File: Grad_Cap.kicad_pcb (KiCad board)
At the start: 2 copper layers, 2 parts, among them U1 Itsy_NRF

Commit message: Cleaning files
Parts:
- moved U1 214.5 mm to (233.4, 216.5)
- moved D1 22.8 mm to (92.5, 45.5)
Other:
- board outline added: 240 x 240 mm
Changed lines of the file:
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@@
     (thickness 1.6)
   )
-  (paper "A4")
+  (paper "A3")
   (layers
     (0 "F.Cu" signal)
@@
   (net 31 "VBUS")
   (footprint "LED_SMD:LED_Inolux_IN-PI554FCH_PLCC4_5.0x5.0mm_P3.2mm" (layer "F.Cu")
-    (at 103.5 65.5)
+    (at 92.5 45.5)
     (descr "http://www.inolux-corp.com/datasheet/SMDLED/Addressable%20LED/IN-PI554FCH.pdf")
     (tags "RGB LED NeoPixel addressable")
@@
   )
   (footprint "Package_DIP:DIP-28_W15.24mm_LongPads" (layer "F.Cu")
-    (at 82.3 64.3)
+    (at 233.4 216.5)
     (descr "28-lead though-hole mounted DIP package, row spacing 15.24 mm (600 mils), LongPads")
     (tags "THT DIP DIL PDIP 2.54mm 15.24mm 600mil LongPads")
@@
     )
   )
+  (gr_circle (center 140 140) (end 160 140) (layer "Edge.Cuts") (width 0.1) (fill none))
+  (gr_rect (start 20 20) (end 260 260) (layer "Edge.Cuts") (width 0.1) (fill none))
 )

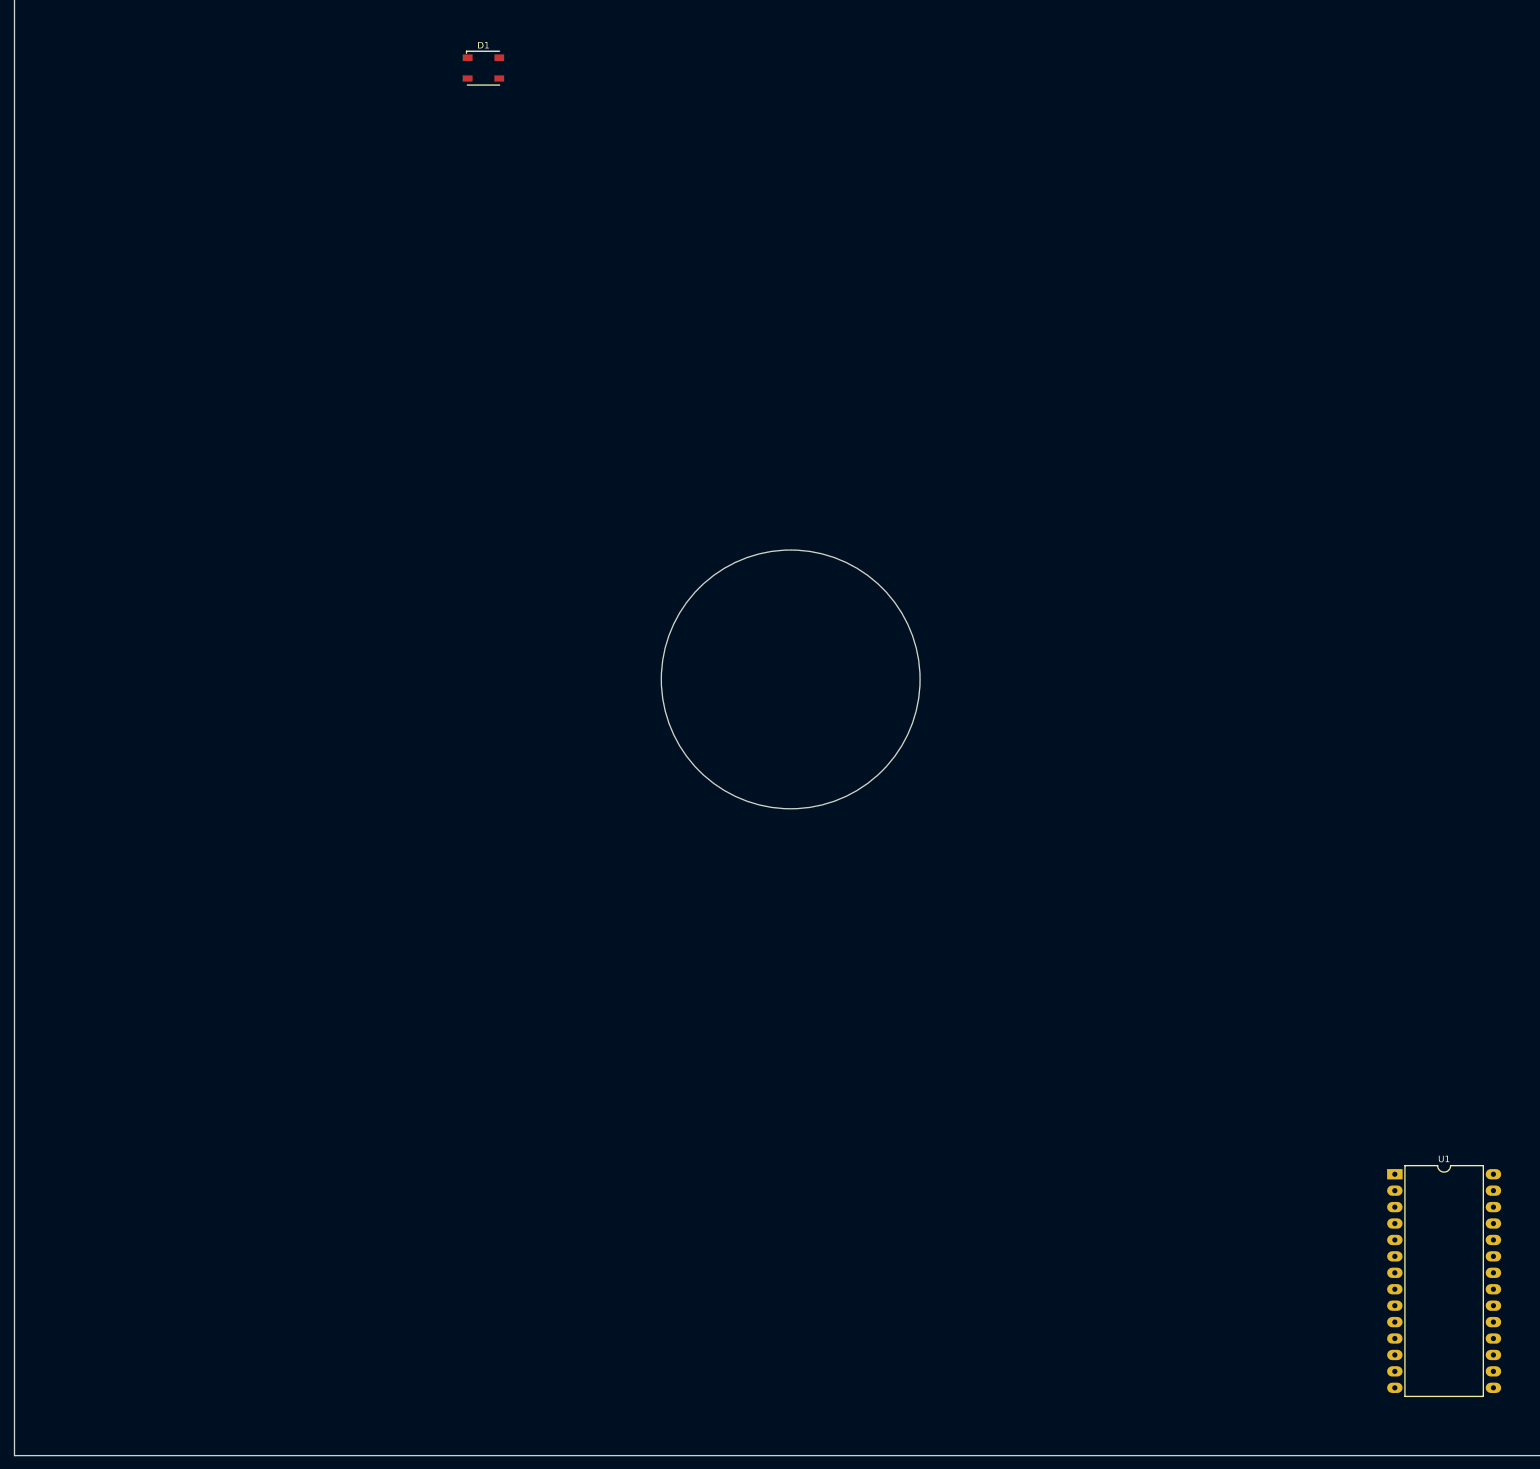
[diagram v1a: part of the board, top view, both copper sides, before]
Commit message: Added neopixels
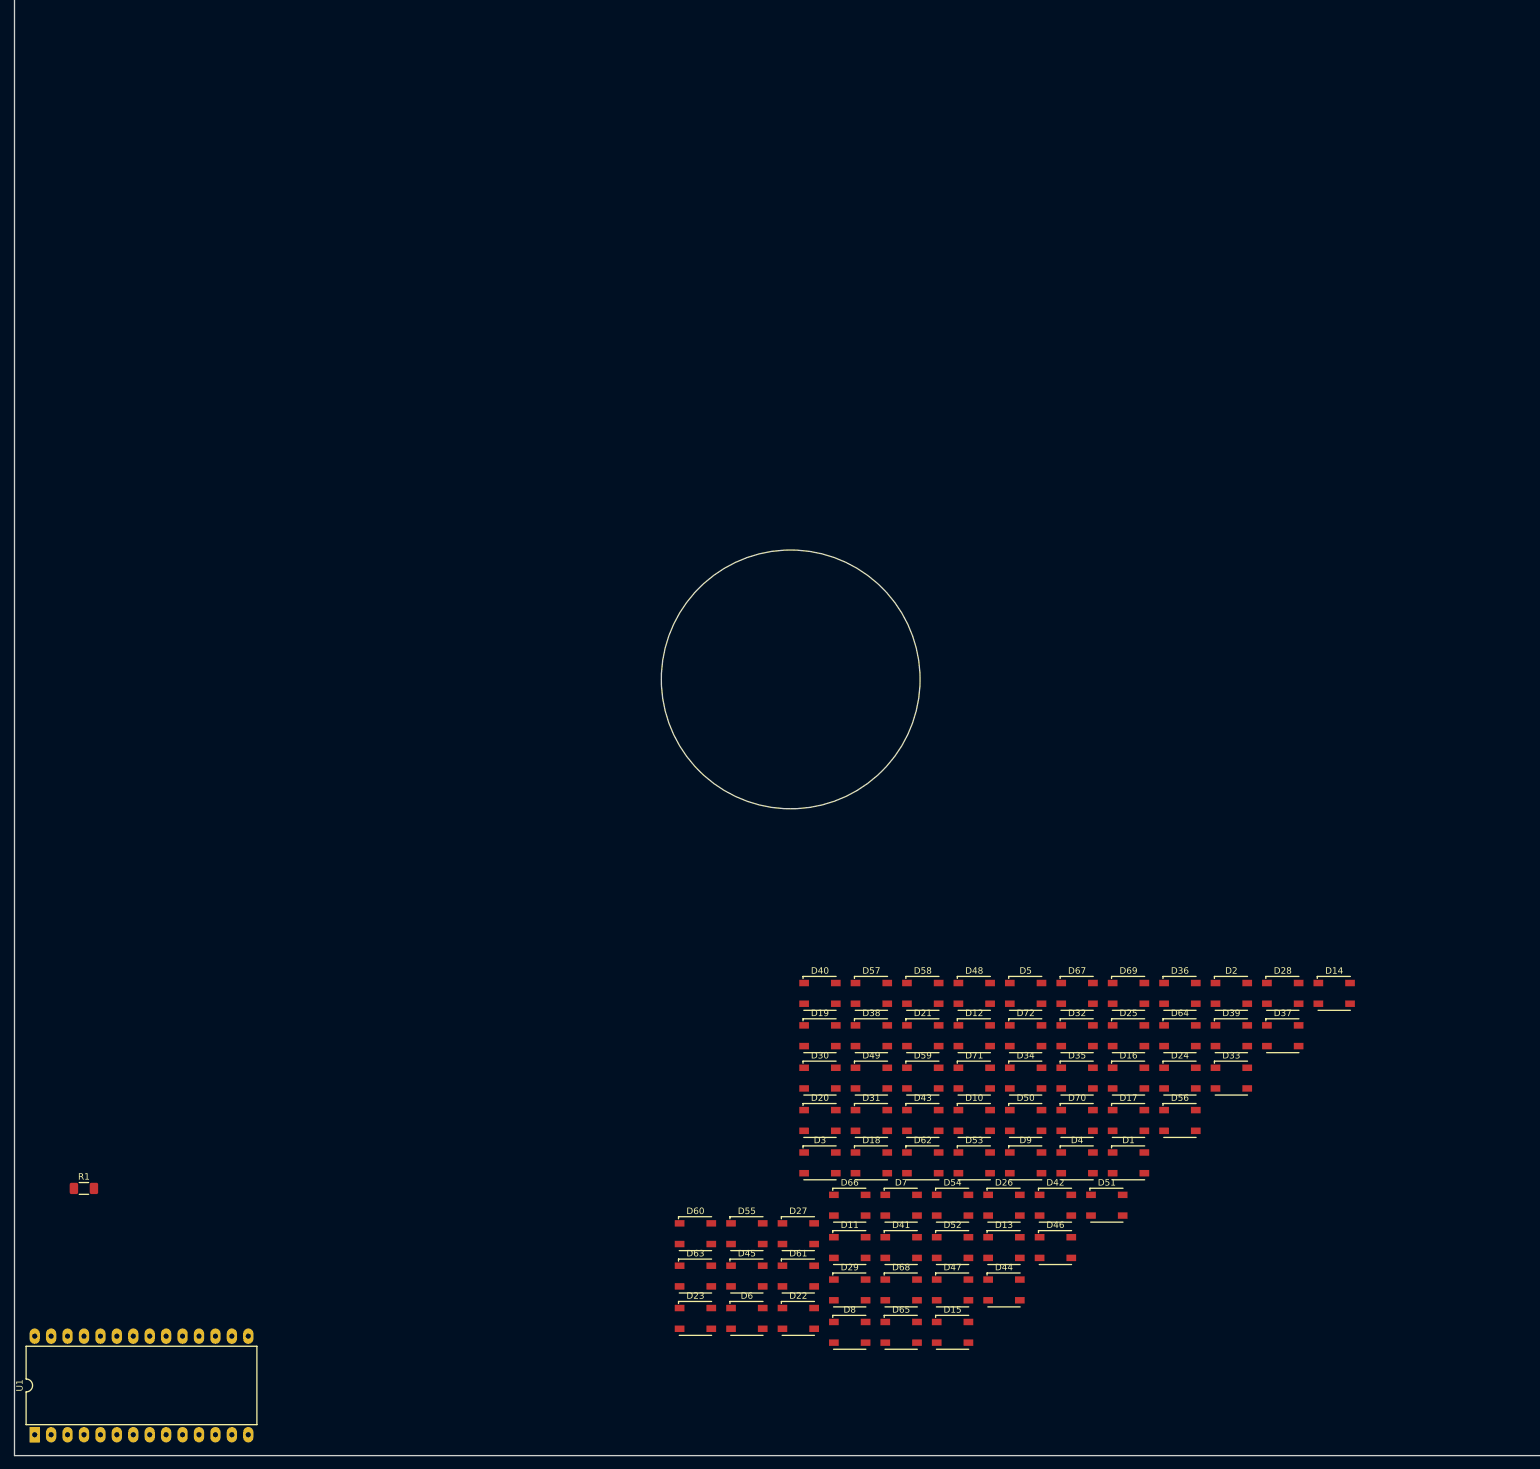
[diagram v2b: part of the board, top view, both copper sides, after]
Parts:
- added D10: Neopixel 5050, LED_SMD:LED_Inolux_IN-PI554FCH_PLCC4_5.0x5.0mm_P3.2mm, F.Cu at (168.4, 208.2)
- added D11: Neopixel 5050, LED_SMD:LED_Inolux_IN-PI554FCH_PLCC4_5.0x5.0mm_P3.2mm, F.Cu at (149.1, 227.8)
- added D12: Neopixel 5050, LED_SMD:LED_Inolux_IN-PI554FCH_PLCC4_5.0x5.0mm_P3.2mm, F.Cu at (168.4, 195.1)
- added D13: Neopixel 5050, LED_SMD:LED_Inolux_IN-PI554FCH_PLCC4_5.0x5.0mm_P3.2mm, F.Cu at (173.0, 227.8)
- added D14: Neopixel 5050, LED_SMD:LED_Inolux_IN-PI554FCH_PLCC4_5.0x5.0mm_P3.2mm, F.Cu at (224.0, 188.5)
- added D15: Neopixel 5050, LED_SMD:LED_Inolux_IN-PI554FCH_PLCC4_5.0x5.0mm_P3.2mm, F.Cu at (165.0, 240.9)
- added D16: Neopixel 5050, LED_SMD:LED_Inolux_IN-PI554FCH_PLCC4_5.0x5.0mm_P3.2mm, F.Cu at (192.2, 201.6)
- added D17: Neopixel 5050, LED_SMD:LED_Inolux_IN-PI554FCH_PLCC4_5.0x5.0mm_P3.2mm, F.Cu at (192.2, 208.2)
- added D18: Neopixel 5050, LED_SMD:LED_Inolux_IN-PI554FCH_PLCC4_5.0x5.0mm_P3.2mm, F.Cu at (152.5, 214.7)
- added D19: Neopixel 5050, LED_SMD:LED_Inolux_IN-PI554FCH_PLCC4_5.0x5.0mm_P3.2mm, F.Cu at (144.5, 195.1)
- added D2: Neopixel 5050, LED_SMD:LED_Inolux_IN-PI554FCH_PLCC4_5.0x5.0mm_P3.2mm, F.Cu at (208.1, 188.5)
- added D20: Neopixel 5050, LED_SMD:LED_Inolux_IN-PI554FCH_PLCC4_5.0x5.0mm_P3.2mm, F.Cu at (144.5, 208.2)
- added D21: Neopixel 5050, LED_SMD:LED_Inolux_IN-PI554FCH_PLCC4_5.0x5.0mm_P3.2mm, F.Cu at (160.4, 195.1)
- added D22: Neopixel 5050, LED_SMD:LED_Inolux_IN-PI554FCH_PLCC4_5.0x5.0mm_P3.2mm, F.Cu at (141.2, 238.8)
- added D23: Neopixel 5050, LED_SMD:LED_Inolux_IN-PI554FCH_PLCC4_5.0x5.0mm_P3.2mm, F.Cu at (125.3, 238.8)
- added D24: Neopixel 5050, LED_SMD:LED_Inolux_IN-PI554FCH_PLCC4_5.0x5.0mm_P3.2mm, F.Cu at (200.2, 201.6)
- added D25: Neopixel 5050, LED_SMD:LED_Inolux_IN-PI554FCH_PLCC4_5.0x5.0mm_P3.2mm, F.Cu at (192.2, 195.1)
- added D26: Neopixel 5050, LED_SMD:LED_Inolux_IN-PI554FCH_PLCC4_5.0x5.0mm_P3.2mm, F.Cu at (173.0, 221.3)
- added D27: Neopixel 5050, LED_SMD:LED_Inolux_IN-PI554FCH_PLCC4_5.0x5.0mm_P3.2mm, F.Cu at (141.2, 225.7)
- added D28: Neopixel 5050, LED_SMD:LED_Inolux_IN-PI554FCH_PLCC4_5.0x5.0mm_P3.2mm, F.Cu at (216.1, 188.5)
- added D29: Neopixel 5050, LED_SMD:LED_Inolux_IN-PI554FCH_PLCC4_5.0x5.0mm_P3.2mm, F.Cu at (149.1, 234.4)
- added D3: Neopixel 5050, LED_SMD:LED_Inolux_IN-PI554FCH_PLCC4_5.0x5.0mm_P3.2mm, F.Cu at (144.5, 214.7)
- added D30: Neopixel 5050, LED_SMD:LED_Inolux_IN-PI554FCH_PLCC4_5.0x5.0mm_P3.2mm, F.Cu at (144.5, 201.6)
- added D31: Neopixel 5050, LED_SMD:LED_Inolux_IN-PI554FCH_PLCC4_5.0x5.0mm_P3.2mm, F.Cu at (152.5, 208.2)
- added D32: Neopixel 5050, LED_SMD:LED_Inolux_IN-PI554FCH_PLCC4_5.0x5.0mm_P3.2mm, F.Cu at (184.3, 195.1)
- added D33: Neopixel 5050, LED_SMD:LED_Inolux_IN-PI554FCH_PLCC4_5.0x5.0mm_P3.2mm, F.Cu at (208.1, 201.6)
- added D34: Neopixel 5050, LED_SMD:LED_Inolux_IN-PI554FCH_PLCC4_5.0x5.0mm_P3.2mm, F.Cu at (176.3, 201.6)
- added D35: Neopixel 5050, LED_SMD:LED_Inolux_IN-PI554FCH_PLCC4_5.0x5.0mm_P3.2mm, F.Cu at (184.3, 201.6)
- added D36: Neopixel 5050, LED_SMD:LED_Inolux_IN-PI554FCH_PLCC4_5.0x5.0mm_P3.2mm, F.Cu at (200.2, 188.5)
- added D37: Neopixel 5050, LED_SMD:LED_Inolux_IN-PI554FCH_PLCC4_5.0x5.0mm_P3.2mm, F.Cu at (216.1, 195.1)
- added D38: Neopixel 5050, LED_SMD:LED_Inolux_IN-PI554FCH_PLCC4_5.0x5.0mm_P3.2mm, F.Cu at (152.5, 195.1)
- added D39: Neopixel 5050, LED_SMD:LED_Inolux_IN-PI554FCH_PLCC4_5.0x5.0mm_P3.2mm, F.Cu at (208.1, 195.1)
- added D4: Neopixel 5050, LED_SMD:LED_Inolux_IN-PI554FCH_PLCC4_5.0x5.0mm_P3.2mm, F.Cu at (184.3, 214.7)
- added D40: Neopixel 5050, LED_SMD:LED_Inolux_IN-PI554FCH_PLCC4_5.0x5.0mm_P3.2mm, F.Cu at (144.5, 188.5)
- added D41: Neopixel 5050, LED_SMD:LED_Inolux_IN-PI554FCH_PLCC4_5.0x5.0mm_P3.2mm, F.Cu at (157.1, 227.8)
- added D42: Neopixel 5050, LED_SMD:LED_Inolux_IN-PI554FCH_PLCC4_5.0x5.0mm_P3.2mm, F.Cu at (180.9, 221.3)
- added D43: Neopixel 5050, LED_SMD:LED_Inolux_IN-PI554FCH_PLCC4_5.0x5.0mm_P3.2mm, F.Cu at (160.4, 208.2)
- added D44: Neopixel 5050, LED_SMD:LED_Inolux_IN-PI554FCH_PLCC4_5.0x5.0mm_P3.2mm, F.Cu at (173.0, 234.4)
- added D45: Neopixel 5050, LED_SMD:LED_Inolux_IN-PI554FCH_PLCC4_5.0x5.0mm_P3.2mm, F.Cu at (133.2, 232.2)
- added D46: Neopixel 5050, LED_SMD:LED_Inolux_IN-PI554FCH_PLCC4_5.0x5.0mm_P3.2mm, F.Cu at (180.9, 227.8)
- added D47: Neopixel 5050, LED_SMD:LED_Inolux_IN-PI554FCH_PLCC4_5.0x5.0mm_P3.2mm, F.Cu at (165.0, 234.4)
- added D48: Neopixel 5050, LED_SMD:LED_Inolux_IN-PI554FCH_PLCC4_5.0x5.0mm_P3.2mm, F.Cu at (168.4, 188.5)
- added D49: Neopixel 5050, LED_SMD:LED_Inolux_IN-PI554FCH_PLCC4_5.0x5.0mm_P3.2mm, F.Cu at (152.5, 201.6)
- added D5: Neopixel 5050, LED_SMD:LED_Inolux_IN-PI554FCH_PLCC4_5.0x5.0mm_P3.2mm, F.Cu at (176.3, 188.5)
- added D50: Neopixel 5050, LED_SMD:LED_Inolux_IN-PI554FCH_PLCC4_5.0x5.0mm_P3.2mm, F.Cu at (176.3, 208.2)
- added D51: Neopixel 5050, LED_SMD:LED_Inolux_IN-PI554FCH_PLCC4_5.0x5.0mm_P3.2mm, F.Cu at (188.9, 221.3)
- added D52: Neopixel 5050, LED_SMD:LED_Inolux_IN-PI554FCH_PLCC4_5.0x5.0mm_P3.2mm, F.Cu at (165.0, 227.8)
- added D53: Neopixel 5050, LED_SMD:LED_Inolux_IN-PI554FCH_PLCC4_5.0x5.0mm_P3.2mm, F.Cu at (168.4, 214.7)
- added D54: Neopixel 5050, LED_SMD:LED_Inolux_IN-PI554FCH_PLCC4_5.0x5.0mm_P3.2mm, F.Cu at (165.0, 221.3)
- added D55: Neopixel 5050, LED_SMD:LED_Inolux_IN-PI554FCH_PLCC4_5.0x5.0mm_P3.2mm, F.Cu at (133.2, 225.7)
- added D56: Neopixel 5050, LED_SMD:LED_Inolux_IN-PI554FCH_PLCC4_5.0x5.0mm_P3.2mm, F.Cu at (200.2, 208.2)
- added D57: Neopixel 5050, LED_SMD:LED_Inolux_IN-PI554FCH_PLCC4_5.0x5.0mm_P3.2mm, F.Cu at (152.5, 188.5)
- added D58: Neopixel 5050, LED_SMD:LED_Inolux_IN-PI554FCH_PLCC4_5.0x5.0mm_P3.2mm, F.Cu at (160.4, 188.5)
- added D59: Neopixel 5050, LED_SMD:LED_Inolux_IN-PI554FCH_PLCC4_5.0x5.0mm_P3.2mm, F.Cu at (160.4, 201.6)
- added D6: Neopixel 5050, LED_SMD:LED_Inolux_IN-PI554FCH_PLCC4_5.0x5.0mm_P3.2mm, F.Cu at (133.2, 238.8)
- added D60: Neopixel 5050, LED_SMD:LED_Inolux_IN-PI554FCH_PLCC4_5.0x5.0mm_P3.2mm, F.Cu at (125.3, 225.7)
- added D61: Neopixel 5050, LED_SMD:LED_Inolux_IN-PI554FCH_PLCC4_5.0x5.0mm_P3.2mm, F.Cu at (141.2, 232.2)
- added D62: Neopixel 5050, LED_SMD:LED_Inolux_IN-PI554FCH_PLCC4_5.0x5.0mm_P3.2mm, F.Cu at (160.4, 214.7)
- added D63: Neopixel 5050, LED_SMD:LED_Inolux_IN-PI554FCH_PLCC4_5.0x5.0mm_P3.2mm, F.Cu at (125.3, 232.2)
- added D64: Neopixel 5050, LED_SMD:LED_Inolux_IN-PI554FCH_PLCC4_5.0x5.0mm_P3.2mm, F.Cu at (200.2, 195.1)
- added D65: Neopixel 5050, LED_SMD:LED_Inolux_IN-PI554FCH_PLCC4_5.0x5.0mm_P3.2mm, F.Cu at (157.1, 240.9)
- added D66: Neopixel 5050, LED_SMD:LED_Inolux_IN-PI554FCH_PLCC4_5.0x5.0mm_P3.2mm, F.Cu at (149.1, 221.3)
- added D67: Neopixel 5050, LED_SMD:LED_Inolux_IN-PI554FCH_PLCC4_5.0x5.0mm_P3.2mm, F.Cu at (184.3, 188.5)
- added D68: Neopixel 5050, LED_SMD:LED_Inolux_IN-PI554FCH_PLCC4_5.0x5.0mm_P3.2mm, F.Cu at (157.1, 234.4)
- added D69: Neopixel 5050, LED_SMD:LED_Inolux_IN-PI554FCH_PLCC4_5.0x5.0mm_P3.2mm, F.Cu at (192.2, 188.5)
- added D7: Neopixel 5050, LED_SMD:LED_Inolux_IN-PI554FCH_PLCC4_5.0x5.0mm_P3.2mm, F.Cu at (157.1, 221.3)
- added D70: Neopixel 5050, LED_SMD:LED_Inolux_IN-PI554FCH_PLCC4_5.0x5.0mm_P3.2mm, F.Cu at (184.3, 208.2)
- added D71: Neopixel 5050, LED_SMD:LED_Inolux_IN-PI554FCH_PLCC4_5.0x5.0mm_P3.2mm, F.Cu at (168.4, 201.6)
- added D72: Neopixel 5050, LED_SMD:LED_Inolux_IN-PI554FCH_PLCC4_5.0x5.0mm_P3.2mm, F.Cu at (176.3, 195.1)
- added D8: Neopixel 5050, LED_SMD:LED_Inolux_IN-PI554FCH_PLCC4_5.0x5.0mm_P3.2mm, F.Cu at (149.1, 240.9)
- added D9: Neopixel 5050, LED_SMD:LED_Inolux_IN-PI554FCH_PLCC4_5.0x5.0mm_P3.2mm, F.Cu at (176.3, 214.7)
- added R1: 330, Resistor_SMD:R_1206_3216Metric_Pad1.30x1.75mm_HandSolder, F.Cu at (30.7, 218.7)
- D1: value Inolux_IN-PI554FCH -> Neopixel 5050
- U1: value Itsy_NRF -> ItsyBitsy 32u4 5V
- moved U1 214.1 mm to (23.1, 256.8), turned to 90 degrees
- moved D1 196.4 mm to (192.2, 214.7)
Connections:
- D1 pad 2: unconnected-(D1-Pad2) -> Net-(D1-Pad2)
- D1 pad 3: unconnected-(D1-Pad3) -> +5V
- D1 pad 4: unconnected-(D1-Pad4) -> Net-(D1-Pad4)
- U1 pad 2: unconnected-(U1-Pad2) -> +5V
- U1 pad 25: unconnected-(U1-Pad25) -> Net-(U1-Pad25)
- U1 pad 28: VBUS -> unconnected-(U1-Pad28)
- U1 pad 4: unconnected-(U1-Pad4) -> GND

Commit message: Test shtuff
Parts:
- removed the D6 at (133.2, 238.8)
- removed the D7 at (157.1, 221.3)
- removed the D8 at (149.1, 240.9)
- removed the D9 at (176.3, 214.7)
- added D6: Neopixel 5050, LED_SMD:LED_Inolux_IN-PI554FCH_PLCC4_5.0x5.0mm_P3.2mm, F.Cu at (196.4, 250.4)
- added D6: Neopixel 5050, LED_SMD:LED_Inolux_IN-PI554FCH_PLCC4_5.0x5.0mm_P3.2mm, F.Cu at (196.4, 219.6)
- added D7: Neopixel 5050, LED_SMD:LED_Inolux_IN-PI554FCH_PLCC4_5.0x5.0mm_P3.2mm, F.Cu at (196.4, 212.0)
- added D7: Neopixel 5050, LED_SMD:LED_Inolux_IN-PI554FCH_PLCC4_5.0x5.0mm_P3.2mm, F.Cu at (196.4, 242.8)
- added D8: Neopixel 5050, LED_SMD:LED_Inolux_IN-PI554FCH_PLCC4_5.0x5.0mm_P3.2mm, F.Cu at (196.4, 235.2)
- added D8: Neopixel 5050, LED_SMD:LED_Inolux_IN-PI554FCH_PLCC4_5.0x5.0mm_P3.2mm, F.Cu at (196.4, 204.4)
- added D9: Neopixel 5050, LED_SMD:LED_Inolux_IN-PI554FCH_PLCC4_5.0x5.0mm_P3.2mm, F.Cu at (196.4, 227.6)
- added D9: Neopixel 5050, LED_SMD:LED_Inolux_IN-PI554FCH_PLCC4_5.0x5.0mm_P3.2mm, F.Cu at (196.4, 196.8)
- added G***: LOGO, LOGO, F.Cu at (185.0, 185.0)
- moved D44 269.0 mm to (16.0, 16.0)
- moved D37 268.5 mm to (16.0, 16.0)
- moved D46 268.5 mm to (16.0, 16.0)
- moved D51 268.4 mm to (16.0, 16.0)
- moved D56 266.2 mm to (16.0, 16.0)
- moved D65 265.5 mm to (16.0, 16.0)
- moved D47 264.4 mm to (16.0, 16.0)
- moved D42 263.3 mm to (16.0, 16.0)
- moved D39 262.6 mm to (16.0, 16.0)
- moved D68 260.0 mm to (16.0, 16.0)
- moved D52 259.0 mm to (16.0, 16.0)
- moved D64 256.9 mm to (16.0, 16.0)
- moved D70 255.4 mm to (16.0, 16.0)
- moved D41 254.5 mm to (16.0, 16.0)
- moved D54 253.7 mm to (16.0, 16.0)
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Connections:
- D2 pad 1: GND -> (no net)
- D2 pad 2: Net-(D1-Pad4) -> (no net)
- D2 pad 3: +5V -> (no net)
- D2 pad 4: Net-(D2-Pad4) -> (no net)
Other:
- board size 240 x 240 mm -> 339.4 x 339.4 mm

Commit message: Initial Layout done
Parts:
- removed D18, D2, D26, D34, D42, D47, D50, D53, D6 (x2), D72: Neopixel 5050, LED_SMD:LED_Inolux_IN-PI554FCH_PLCC4_5.0x5.0mm_P3.2mm
- removed the D9 at (196.4, 196.8)
- added D1: Neopixel 5050, LED_SMD:LED_Inolux_IN-PI554FCH_PLCC4_5.0x5.0mm_P3.2mm, F.Cu at (166.5, 175.5)
- added D1: Neopixel 5050, LED_SMD:LED_Inolux_IN-PI554FCH_PLCC4_5.0x5.0mm_P3.2mm, F.Cu at (166.5, 185.1)
- added D48: Neopixel 5050, LED_SMD:LED_Inolux_IN-PI554FCH_PLCC4_5.0x5.0mm_P3.2mm, F.Cu at (123.5, 120.5)
- added D65: Neopixel 5050, LED_SMD:LED_Inolux_IN-PI554FCH_PLCC4_5.0x5.0mm_P3.2mm, F.Cu at (204.6, 166.0)
- added D65: Neopixel 5050, LED_SMD:LED_Inolux_IN-PI554FCH_PLCC4_5.0x5.0mm_P3.2mm, F.Cu at (166.5, 166.0)
- added D66: Neopixel 5050, LED_SMD:LED_Inolux_IN-PI554FCH_PLCC4_5.0x5.0mm_P3.2mm, F.Cu at (230.0, 166.0)
- added D66: Neopixel 5050, LED_SMD:LED_Inolux_IN-PI554FCH_PLCC4_5.0x5.0mm_P3.2mm, F.Cu at (191.9, 166.0)
- added D67: Neopixel 5050, LED_SMD:LED_Inolux_IN-PI554FCH_PLCC4_5.0x5.0mm_P3.2mm, F.Cu at (242.8, 166.0)
- added D7: Neopixel 5050, LED_SMD:LED_Inolux_IN-PI554FCH_PLCC4_5.0x5.0mm_P3.2mm, F.Cu at (255.5, 185.0)
- added D7: Neopixel 5050, LED_SMD:LED_Inolux_IN-PI554FCH_PLCC4_5.0x5.0mm_P3.2mm, F.Cu at (224.8, 219.7)
- added D8: Neopixel 5050, LED_SMD:LED_Inolux_IN-PI554FCH_PLCC4_5.0x5.0mm_P3.2mm, F.Cu at (255.5, 175.5)
- added D8: Neopixel 5050, LED_SMD:LED_Inolux_IN-PI554FCH_PLCC4_5.0x5.0mm_P3.2mm, F.Cu at (224.8, 208.1)
- added D8: Neopixel 5050, LED_SMD:LED_Inolux_IN-PI554FCH_PLCC4_5.0x5.0mm_P3.2mm, F.Cu at (224.8, 231.2)
- added D9: Neopixel 5050, LED_SMD:LED_Inolux_IN-PI554FCH_PLCC4_5.0x5.0mm_P3.2mm, F.Cu at (255.5, 194.6)
- added D9: Neopixel 5050, LED_SMD:LED_Inolux_IN-PI554FCH_PLCC4_5.0x5.0mm_P3.2mm, F.Cu at (224.8, 196.6)
- added D9: Neopixel 5050, LED_SMD:LED_Inolux_IN-PI554FCH_PLCC4_5.0x5.0mm_P3.2mm, F.Cu at (255.5, 204.2)
- added D9: Neopixel 5050, LED_SMD:LED_Inolux_IN-PI554FCH_PLCC4_5.0x5.0mm_P3.2mm, F.Cu at (255.5, 166.0)
- added D9: Neopixel 5050, LED_SMD:LED_Inolux_IN-PI554FCH_PLCC4_5.0x5.0mm_P3.2mm, F.Cu at (240.1, 196.6)
- added D9: Neopixel 5050, LED_SMD:LED_Inolux_IN-PI554FCH_PLCC4_5.0x5.0mm_P3.2mm, F.Cu at (217.3, 166.0)
- added D9: Neopixel 5050, LED_SMD:LED_Inolux_IN-PI554FCH_PLCC4_5.0x5.0mm_P3.2mm, F.Cu at (240.2, 204.2)
- added D9: Neopixel 5050, LED_SMD:LED_Inolux_IN-PI554FCH_PLCC4_5.0x5.0mm_P3.2mm, F.Cu at (179.2, 166.0)
- moved D67 342.5 mm to (232.4, 281.4)
- moved D68 334.9 mm to (232.4, 271.6)
- moved D66 333.5 mm to (217.9, 281.4)
- moved D69 325.6 mm to (224.8, 265.8)
- moved D65 324.9 mm to (203.3, 281.4)
- moved D70 316.8 mm to (224.8, 254.3)
- moved D71 308.2 mm to (224.8, 242.7)
- moved D64 264.2 mm to (181.4, 222.0)
- moved D63 259.2 mm to (169.7, 224.8)
- moved D62 253.1 mm to (159.0, 224.8)
- moved D61 244.8 mm to (148.0, 222.2)
- moved D60 235.6 mm to (136.6, 218.3)
- moved D59 225.9 mm to (127.8, 212.3)
- moved D35 224.4 mm to (217.1, 115.5)
- moved U1 221.7 mm to (195.7, 332.1), turned to -135 degrees
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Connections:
- D11 pad 1: GND -> (no net)
- D11 pad 2: Net-(D10-Pad4) -> (no net)
- D11 pad 3: +5V -> (no net)
- D11 pad 4: Net-(D11-Pad4) -> (no net)
- D23 pad 1: GND -> (no net)
- D23 pad 2: Net-(D22-Pad4) -> (no net)
- D23 pad 3: +5V -> (no net)
- D23 pad 4: Net-(D23-Pad4) -> (no net)

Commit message: It looks pretty
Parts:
- added G***: LOGO, LOGO, F.Cu at (185.0, 185.0)
- moved U1 70.3 mm to (218.6, 265.7), turned to 180 degrees
